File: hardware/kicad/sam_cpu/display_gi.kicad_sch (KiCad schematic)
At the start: 4 parts, among them J18 J18 GI DIMMER

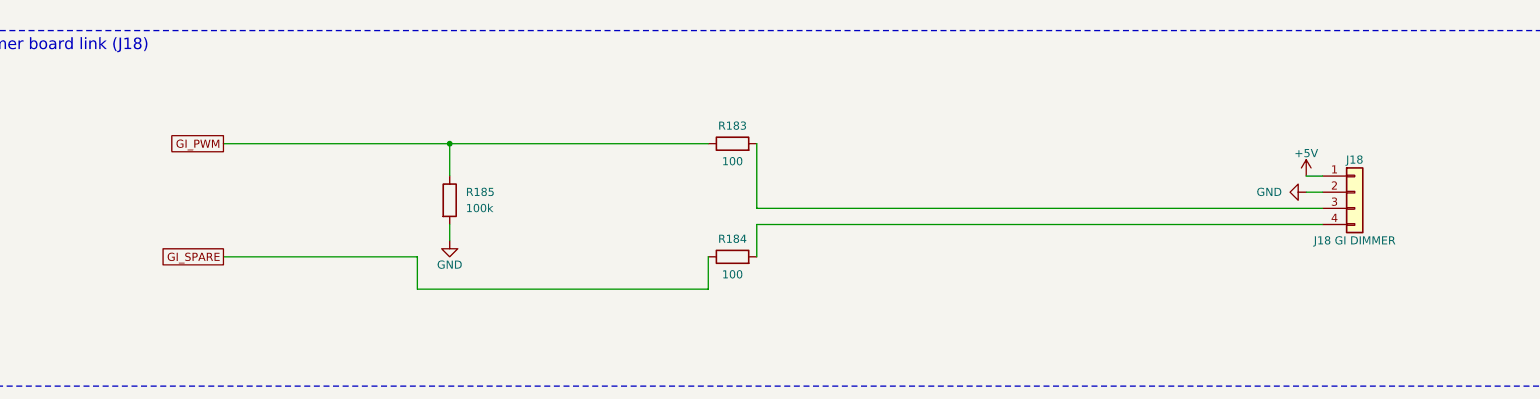
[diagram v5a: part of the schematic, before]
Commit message: DIP switch block not loaded; larger schematic text
c30: SW3, R168-R175, U14 and C93 flagged DNP (schematic and board).
c31: schematic text 1.27 -> 1.6 mm (pins 1.5 mm), intersheet refs moved out.

Co-Authored-By: Claude Opus 5.5 (1M context) <noreply@anthropic.com>
Claude-Session: https://claude.ai/code/session_01ExuDVoDDDHhVWjb8EwVzYb
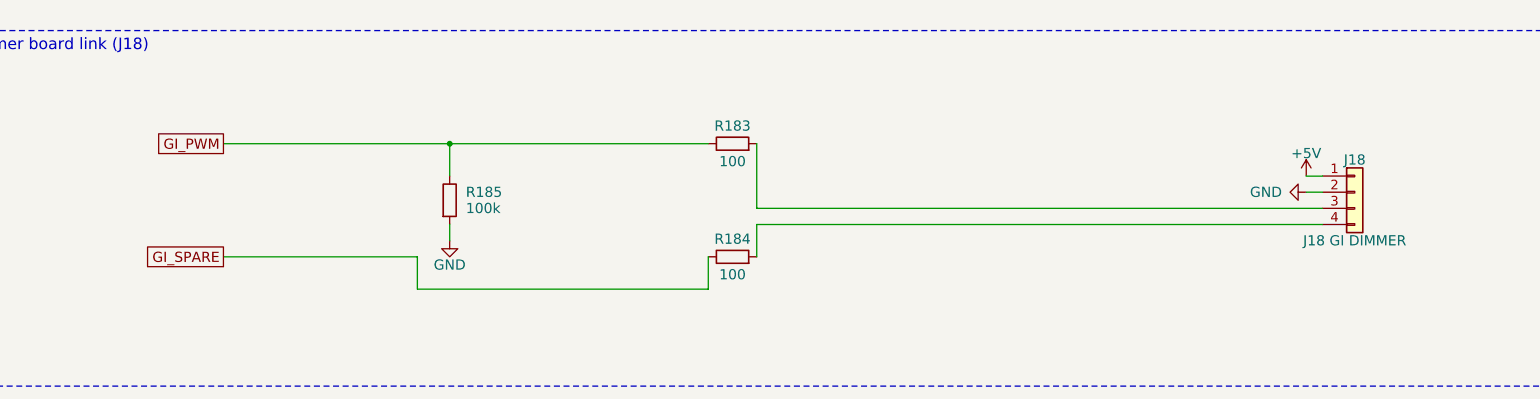
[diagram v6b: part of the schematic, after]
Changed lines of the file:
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@@
 		(effects
 			(font
-				(size 1.27 1.27)
+				(size 1.6 1.6)
 			)
 			(justify right)
 		)
 		(property "Intersheetrefs" "${INTERSHEET_REFS}"
-			(at 62.64 233.68 180)
-			(show_name no)
-			(do_not_autoplace no)
-			(effects
-				(font
-					(size 1.27 1.27)
+			(at 59.12 233.68 180)
+			(show_name no)
+			(do_not_autoplace no)
+			(effects
+				(font
+					(size 1.6 1.6)
 				)
 				(justify right)
@@
 		(effects
 			(font
-				(size 1.27 1.27)
+				(size 1.6 1.6)
 			)
 			(justify right)
 		)
 		(property "Intersheetrefs" "${INTERSHEET_REFS}"
-			(at 65.18 215.9 180)
-			(show_name no)
-			(do_not_autoplace no)
-			(effects
-				(font
-					(size 1.27 1.27)
+			(at 62.32 215.9 180)
+			(show_name no)
+			(do_not_autoplace no)
+			(effects
+				(font
+					(size 1.6 1.6)
 				)
 				(justify right)
@@
 			(effects
 				(font
-					(size 1.27 1.27)
+					(size 1.6 1.6)
 				)
 			)
@@
 			(effects
 				(font
-					(size 1.27 1.27)
+					(size 1.6 1.6)
 				)
 			)
@@
 			(effects
 				(font
-					(size 1.27 1.27)
+					(size 1.6 1.6)
 				)
 			)
@@
 			(effects
 				(font
-					(size 1.27 1.27)
+					(size 1.6 1.6)
 				)
 			)
@@
 			(effects
 				(font
-					(size 1.27 1.27)
+					(size 1.6 1.6)
 				)
 			)
@@
 			(effects
 				(font
-					(size 1.27 1.27)
+					(size 1.6 1.6)
 				)
 			)
@@
 			(effects
 				(font
-					(size 1.27 1.27)
+					(size 1.6 1.6)
 				)
 			)
@@
 			(effects
 				(font
-					(size 1.27 1.27)
+					(size 1.6 1.6)
 				)
 			)
@@
 			(effects
 				(font
-					(size 1.27 1.27)
+					(size 1.6 1.6)
 				)
 			)
@@
 			(effects
 				(font
-					(size 1.27 1.27)
+					(size 1.6 1.6)
 				)
 			)
@@
 			(effects
 				(font
-					(size 1.27 1.27)
+					(size 1.6 1.6)
 				)
 			)
@@
 			(effects
 				(font
-					(size 1.27 1.27)
+					(size 1.6 1.6)
 				)
 				(justify right)
@@
 			(effects
 				(font
-					(size 1.27 1.27)
+					(size 1.6 1.6)
 				)
 			)
@@
 			(effects
 				(font
-					(size 1.27 1.27)
+					(size 1.6 1.6)
 				)
 			)
@@
 			(effects
 				(font
-					(size 1.27 1.27)
+					(size 1.6 1.6)
 				)
 			)
@@
 			(effects
 				(font
-					(size 1.27 1.27)
+					(size 1.6 1.6)
 				)
 			)
@@
 			(effects
 				(font
-					(size 1.27 1.27)
+					(size 1.6 1.6)
 				)
 			)
@@
 			(effects
 				(font
-					(size 1.27 1.27)
+					(size 1.6 1.6)
 				)
 			)
@@
 			(effects
 				(font
-					(size 1.27 1.27)
+					(size 1.6 1.6)
 				)
 			)
@@
 			(effects
 				(font
-					(size 1.27 1.27)
+					(size 1.6 1.6)
 				)
 			)
@@
 			(effects
 				(font
-					(size 1.27 1.27)
+					(size 1.6 1.6)
 				)
 			)
@@
 			(effects
 				(font
-					(size 1.27 1.27)
+					(size 1.6 1.6)
 				)
 			)
@@
 			(effects
 				(font
-					(size 1.27 1.27)
+					(size 1.6 1.6)
 				)
 			)
@@
 			(effects
 				(font
-					(size 1.27 1.27)
+					(size 1.6 1.6)
 				)
 			)
@@
 			(effects
 				(font
-					(size 1.27 1.27)
+					(size 1.6 1.6)
 				)
 			)
@@
 			(effects
 				(font
-					(size 1.27 1.27)
+					(size 1.6 1.6)
 				)
 			)
@@
 			(effects
 				(font
-					(size 1.27 1.27)
+					(size 1.6 1.6)
 				)
 			)
@@
 			(effects
 				(font
-					(size 1.27 1.27)
+					(size 1.6 1.6)
 				)
 			)
@@
 			(effects
 				(font
-					(size 1.27 1.27)
+					(size 1.6 1.6)
 				)
 			)
@@
 			(effects
 				(font
-					(size 1.27 1.27)
+					(size 1.6 1.6)
 				)
 			)
@@
 			(effects
 				(font
-					(size 1.27 1.27)
+					(size 1.6 1.6)
 				)
 				(justify left)
@@
 			(effects
 				(font
-					(size 1.27 1.27)
+					(size 1.6 1.6)
 				)
 				(justify left)
@@
 			(effects
 				(font
-					(size 1.27 1.27)
+					(size 1.6 1.6)
 				)
 			)
@@
 			(effects
 				(font
-					(size 1.27 1.27)
+					(size 1.6 1.6)
 				)
 			)
@@
 			(effects
 				(font
-					(size 1.27 1.27)
-				)
-			)
+					(size 1.6 1.6)
+				)
+			)
